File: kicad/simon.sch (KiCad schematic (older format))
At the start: 20 parts, among them IC1 ATMEGA328P-PU, SW1 Reset, SW2 SW_PUSH, SW3 SW_PUSH, SW4 SW_PUSH, SW5 SW_PUSH, Y1 16MHz

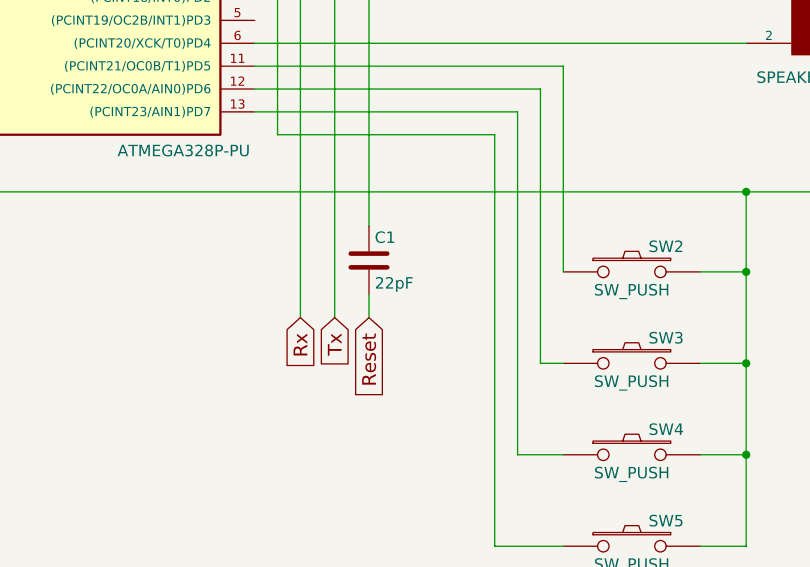
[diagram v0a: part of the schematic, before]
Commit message: rest capacitor 22pF -> 100nF
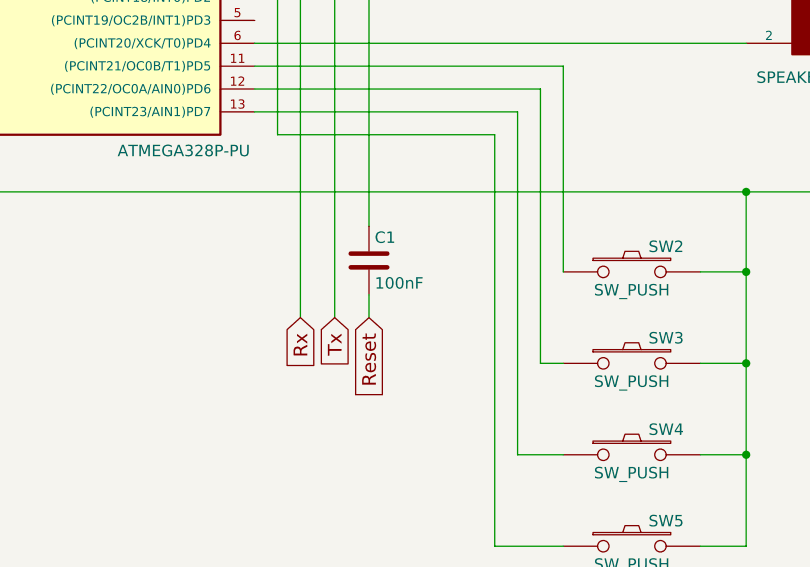
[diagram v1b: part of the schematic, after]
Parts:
- C1: value 22pF -> 100nF
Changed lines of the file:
@@
 Sheet 1 1
 Title "Simon"
-Date "2016-01-03"
-Rev "0.1"
+Date "2016-03-25"
+Rev "0.2"
 Comp ""
 Comment1 ""
@@
 P 3950 4950
 F 0 "C1" H 3975 5050 50  0000 L CNN
-F 1 "22pF" H 3975 4850 50  0000 L CNN
+F 1 "100nF" H 3975 4850 50  0000 L CNN
 F 2 "" H 3988 4800 50  0000 C CNN
 F 3 "" H 3950 4950 50  0000 C CNN

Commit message: reset resistor 1k -> 10k
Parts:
- D1, D2, D3, D4: symbol LED -> LED-RESCUE-simon
- R1: value 1KΩ -> 10KΩ
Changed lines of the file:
@@
 EESchema Schematic File Version 2
+LIBS:simon-rescue
 LIBS:power
 LIBS:device
@@
 $EndComp
 $Comp
-L LED D1
+L LED-RESCUE-simon D1
 U 1 1 5682C58C
 P 6500 2100
@@
 $EndComp
 $Comp
-L LED D2
+L LED-RESCUE-simon D2
 U 1 1 5682C66F
 P 6500 2400
@@
 $EndComp
 $Comp
-L LED D3
+L LED-RESCUE-simon D3
 U 1 1 5682C6A8
 P 6500 2700
@@
 $EndComp
 $Comp
-L LED D4
+L LED-RESCUE-simon D4
 U 1 1 5682C6DA
 P 6500 3000
@@
 P 2450 1600
 F 0 "R1" V 2530 1600 50  0000 C CNN
-F 1 "1KΩ" V 2450 1600 50  0000 C CNN
+F 1 "10KΩ" V 2450 1600 50  0000 C CNN
 F 2 "" V 2380 1600 50  0000 C CNN
 F 3 "" H 2450 1600 50  0000 C CNN
